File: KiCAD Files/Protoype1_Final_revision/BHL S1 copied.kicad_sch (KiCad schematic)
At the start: 94 parts, among them IC1 NUP2105LT1G, IC2 NUP2105LT1G, IC3 IR2136STRPBF, J2 Conn_01x03_Pin, J3 Conn_01x03_Pin, Q1 CSD19502Q5B, Q2 CSD19502Q5B, Q3 CSD19502Q5B, Q4 CSD19502Q5B, Q5 CSD19502Q5B, Q7 CSD19502Q5B, U1 ME6211C30M5, U2 SPX3819M5-L-5-0, U3 Solder Pad, U5 STM32G431CBU6, Y1 8MHz

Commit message: unlocked files
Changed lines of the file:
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@@
 	)
 	(global_label "Curr_fdbk1_OPAmp-"
-		(shape input)
+		(shape passive)
 		(at 45.72 184.15 180)
 		(fields_autoplaced yes)
@@
 		)
 		(property "Intersheetrefs" "${INTERSHEET_REFS}"
-			(at 23.4431 184.15 0)
+			(at 24.5544 184.15 0)
 			(effects
 				(font
@@
 	)
 	(global_label "Vshunt_2-"
-		(shape input)
+		(shape passive)
 		(at 313.69 96.52 180)
 		(fields_autoplaced yes)
@@
 		)
 		(property "Intersheetrefs" "${INTERSHEET_REFS}"
-			(at 300.6659 96.52 0)
+			(at 301.7772 96.52 0)
 			(effects
 				(font
@@
 	)
 	(global_label "Vshunt_3-"
-		(shape input)
+		(shape passive)
 		(at 95.25 194.31 0)
 		(fields_autoplaced yes)
@@
 		)
 		(property "Intersheetrefs" "${INTERSHEET_REFS}"
-			(at 108.2741 194.31 0)
+			(at 107.1628 194.31 0)
 			(effects
 				(font
@@
 	)
 	(global_label "Vshunt_3-"
-		(shape input)
+		(shape passive)
 		(at 340.36 86.36 90)
 		(fields_autoplaced yes)
@@
 		)
 		(property "Intersheetrefs" "${INTERSHEET_REFS}"
-			(at 340.36 73.3359 90)
+			(at 340.36 74.4472 90)
 			(effects
 				(font
@@
 	)
 	(global_label "Vshunt_1-"
-		(shape input)
+		(shape passive)
 		(at 255.27 83.82 180)
 		(fields_autoplaced yes)
@@
 		)
 		(property "Intersheetrefs" "${INTERSHEET_REFS}"
-			(at 242.2459 83.82 0)
+			(at 243.3572 83.82 0)
 			(effects
 				(font
@@
 	)
 	(global_label "Vshunt_2-"
-		(shape input)
+		(shape passive)
 		(at 95.25 189.23 0)
 		(fields_autoplaced yes)
@@
 		)
 		(property "Intersheetrefs" "${INTERSHEET_REFS}"
-			(at 108.2741 189.23 0)
+			(at 107.1628 189.23 0)
 			(effects
 				(font
@@
 	)
 	(global_label "Curr_fdbk1_OPAmp-"
-		(shape input)
+		(shape passive)
 		(at 74.93 66.04 180)
 		(fields_autoplaced yes)
@@
 		)
 		(property "Intersheetrefs" "${INTERSHEET_REFS}"
-			(at 52.6531 66.04 0)
+			(at 53.7644 66.04 0)
 			(effects
 				(font
@@
 	)
 	(global_label "Vshunt_1-"
-		(shape input)
+		(shape passive)
 		(at 95.25 184.15 0)
 		(fields_autoplaced yes)
@@
 		)
 		(property "Intersheetrefs" "${INTERSHEET_REFS}"
-			(at 108.2741 184.15 0)
+			(at 107.1628 184.15 0)
 			(effects
 				(font
@@
 	)
 	(global_label "Curr_fdbk3_OPAmp-"
-		(shape input)
+		(shape passive)
 		(at 45.72 194.31 180)
 		(fields_autoplaced yes)
@@
 		)
 		(property "Intersheetrefs" "${INTERSHEET_REFS}"
-			(at 23.4431 194.31 0)
+			(at 24.5544 194.31 0)
 			(effects
 				(font
@@
 	)
 	(global_label "Curr_fdbk2_OPAmp-"
-		(shape input)
+		(shape passive)
 		(at 45.72 189.23 180)
 		(fields_autoplaced yes)
@@
 		)
 		(property "Intersheetrefs" "${INTERSHEET_REFS}"
-			(at 23.4431 189.23 0)
-			(effects
-				(font
+			(at 24.5544 189.23 0)
+			(effects
+				(font

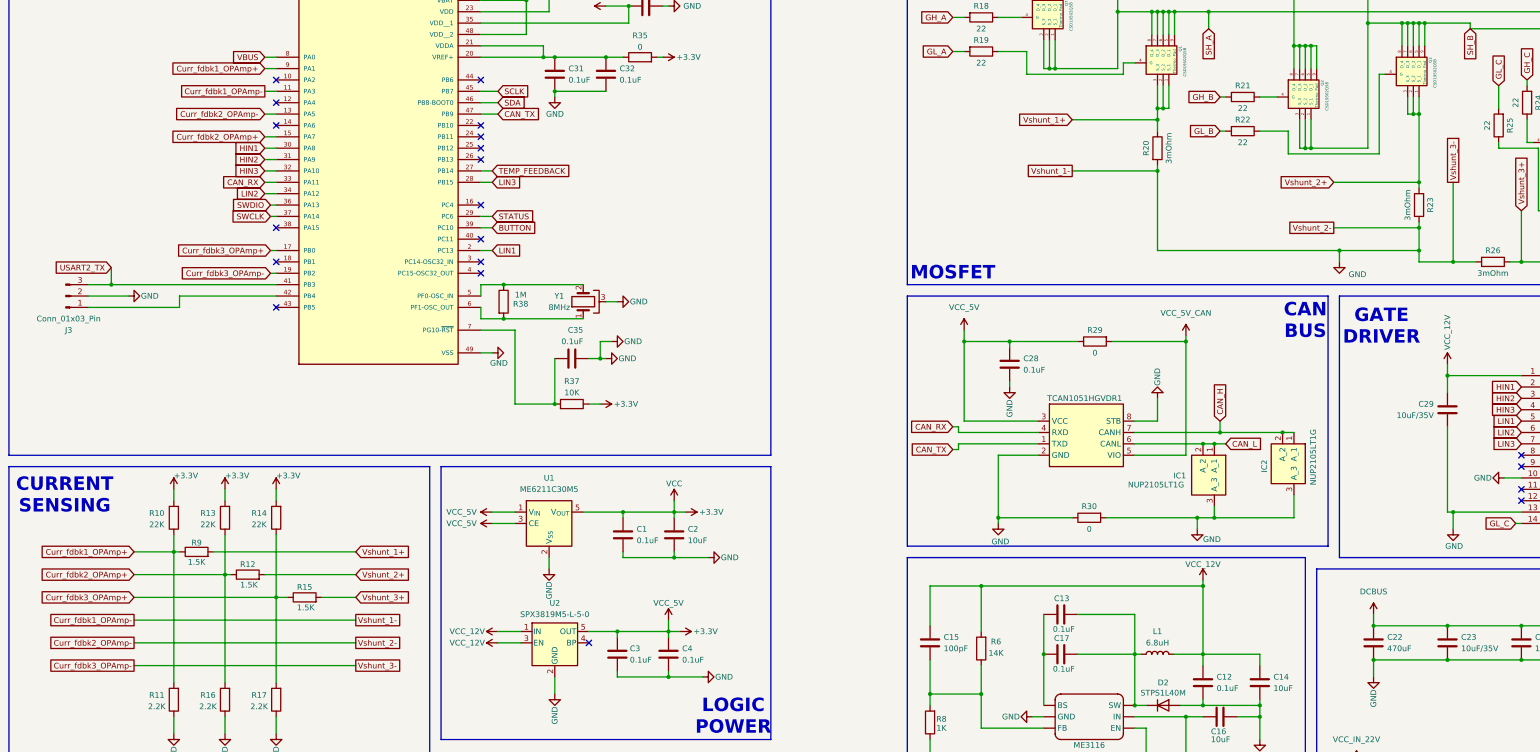
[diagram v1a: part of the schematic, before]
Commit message: Fixed GND Net label issue on PCB creation
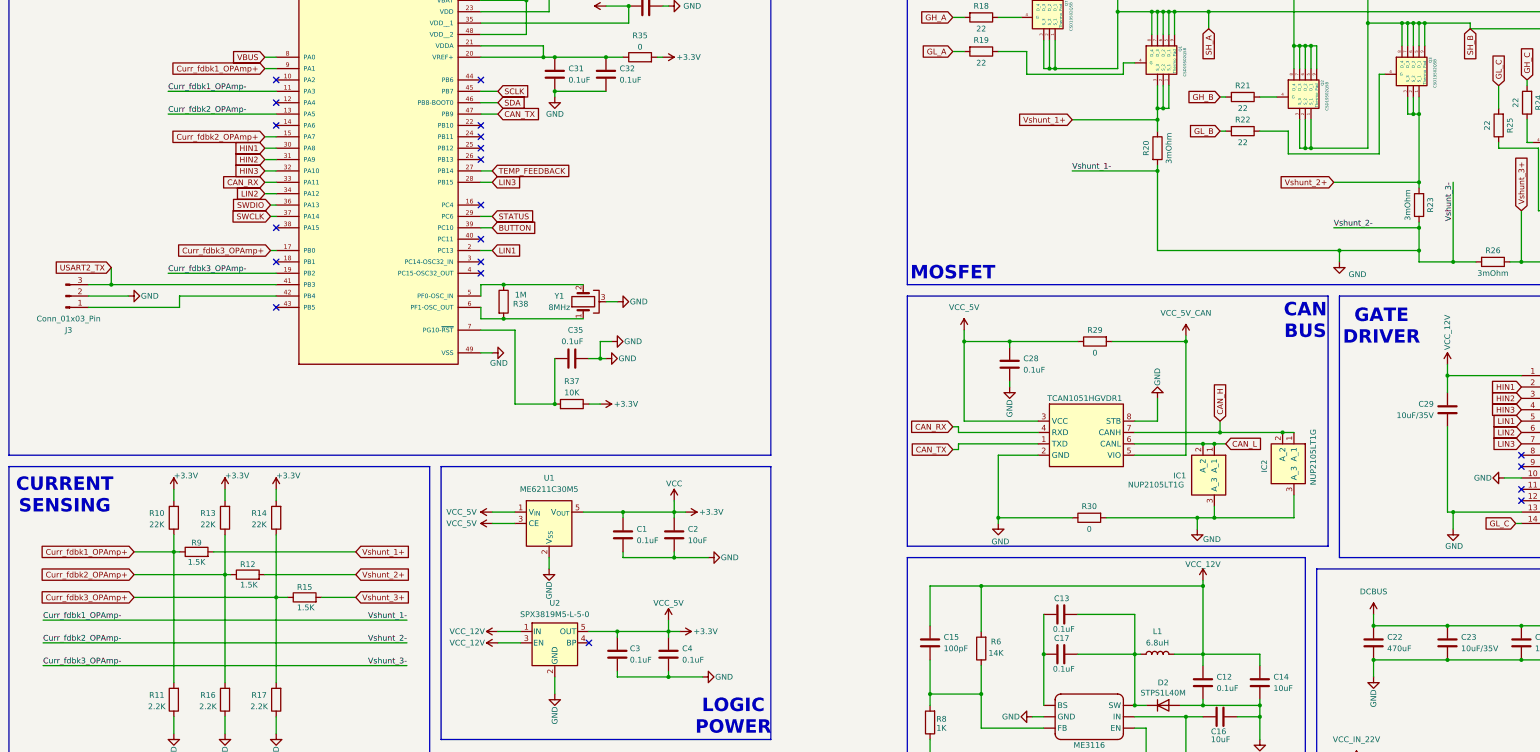
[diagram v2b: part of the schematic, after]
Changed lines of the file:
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@@
 	(wire
 		(pts
+			(xy 25.4 184.15) (xy 106.68 184.15)
+		)
+		(stroke
+			(width 0)
+			(type default)
+		)
+	)
+	(wire
+		(pts
 			(xy 153.67 195.58) (xy 153.67 196.85)
 		)
@@
 	(wire
 		(pts
-			(xy 45.72 189.23) (xy 95.25 189.23)
+			(xy 25.4 189.23) (xy 106.68 189.23)
 		)
 		(stroke
@@
 	(wire
 		(pts
-			(xy 45.72 194.31) (xy 95.25 194.31)
+			(xy 25.4 194.31) (xy 106.68 194.31)
 		)
 		(stroke
@@
 	(wire
 		(pts
-			(xy 45.72 184.15) (xy 95.25 184.15)
-		)
-		(stroke
-			(width 0)
-			(type default)
-		)
-	)
-	(wire
-		(pts
 			(xy 350.52 78.74) (xy 359.41 78.74)
 		)
@@
 	(wire
 		(pts
-			(xy 76.2 106.68) (xy 77.47 106.68)
+			(xy 53.34 106.68) (xy 77.47 106.68)
 		)
 		(stroke
@@
 	(wire
 		(pts
-			(xy 74.93 66.04) (xy 77.47 66.04)
+			(xy 53.34 66.04) (xy 77.47 66.04)
 		)
 		(stroke
@@
 	(wire
 		(pts
-			(xy 74.93 71.12) (xy 77.47 71.12)
+			(xy 53.34 71.12) (xy 77.47 71.12)
 		)
 		(stroke
@@
 		)
 	)
-	(global_label "Curr_fdbk1_OPAmp-"
-		(shape passive)
-		(at 45.72 184.15 180)
-		(fields_autoplaced yes)
+	(label "Vshunt_3-"
+		(at 340.36 86.36 270)
 		(effects
 			(font
 				(size 1.27 1.27)
 			)
-			(justify right)
+			(justify right bottom)
 		)
-		(property "Intersheetrefs" "${INTERSHEET_REFS}"
-			(at 24.5544 184.15 0)
-			(effects
-				(font
-					(size 1.27 1.27)
-				)
-				(justify right)
-				(hide yes)
+	)
+	(label "Curr_fdbk3_OPAmp-"
+		(at 53.34 106.68 0)
+		(effects
+			(font
+				(size 1.27 1.27)
+			)
+			(justify left bottom)
+		)
+	)
+	(label "Curr_fdbk3_OPAmp-"
+		(at 25.4 194.31 0)
+		(effects
+			(font
+				(size 1.27 1.27)
 			)
+			(justify left bottom)
+		)
+	)
+	(label "Curr_fdbk2_OPAmp-"
+		(at 25.4 189.23 0)
+		(effects
+			(font
+				(size 1.27 1.27)
+			)
+			(justify left bottom)
+		)
+	)
+	(label "Curr_fdbk1_OPAmp-"
+		(at 25.4 184.15 0)
+		(effects
+			(font
+				(size 1.27 1.27)
+			)
+			(justify left bottom)
+		)
+	)
+	(label "Curr_fdbk2_OPAmp-"
+		(at 53.34 71.12 0)
+		(effects
+			(font
+				(size 1.27 1.27)
+			)
+			(justify left bottom)
+		)
+	)
+	(label "Vshunt_1-"
+		(at 255.27 83.82 0)
+		(effects
+			(font
+				(size 1.27 1.27)
+			)
+			(justify left bottom)
+		)
+	)
+	(label "Vshunt_3-"
+		(at 106.68 194.31 180)
+		(effects
+			(font
+				(size 1.27 1.27)
+			)
+			(justify right bottom)
+		)
+	)
+	(label "Vshunt_1-"
+		(at 106.68 184.15 180)
+		(effects
+			(font
+				(size 1.27 1.27)
+			)
+			(justify right bottom)
+		)
+	)
+	(label "Vshunt_2-"
+		(at 313.69 96.52 0)
+		(effects
+			(font
+				(size 1.27 1.27)
+			)
+			(justify left bottom)
+		)
+	)
+	(label "Vshunt_2-"
+		(at 106.68 189.23 180)
+		(effects
+			(font
+				(size 1.27 1.27)
+			)
+			(justify right bottom)
+		)
+	)
+	(label "Curr_fdbk1_OPAmp-"
+		(at 53.34 66.04 0)
+		(effects
+			(font
+				(size 1.27 1.27)
+			)
+			(justify left bottom)
 		)
 	)
@@
 		)
 	)
-	(global_label "Vshunt_2-"
-		(shape passive)
-		(at 313.69 96.52 180)
-		(fields_autoplaced yes)
-		(effects
-			(font
-				(size 1.27 1.27)
-			)
-			(justify right)
-		)
-		(property "Intersheetrefs" "${INTERSHEET_REFS}"
-			(at 301.7772 96.52 0)
-			(effects
-				(font
-					(size 1.27 1.27)
-				)
-				(justify right)
-				(hide yes)
-			)
-		)
-	)
 	(global_label "SWCLK"
 		(shape input)
@@
 		)
 	)
-	(global_label "Vshunt_3-"
-		(shape passive)
-		(at 95.25 194.31 0)
-		(fields_autoplaced yes)
-		(effects
-			(font
-				(size 1.27 1.27)
-			)
-			(justify left)
-		)
-		(property "Intersheetrefs" "${INTERSHEET_REFS}"
-			(at 107.1628 194.31 0)
-			(effects
-				(font
-					(size 1.27 1.27)
-				)
-				(justify left)
-				(hide yes)
-			)
-		)
-	)
 	(global_label "VB3"
 		(shape input)
@@
 		)
 	)
-	(global_label "Vshunt_3-"
-		(shape passive)
-		(at 340.36 86.36 90)
-		(fields_autoplaced yes)
-		(effects
-			(font
-				(size 1.27 1.27)
-			)
-			(justify left)
-		)
-		(property "Intersheetrefs" "${INTERSHEET_REFS}"
-			(at 340.36 74.4472 90)
-			(effects
-				(font
-					(size 1.27 1.27)
-				)
-				(justify left)
-				(hide yes)
-			)
-		)
-	)
 	(global_label "Curr_fdbk2_OPAmp+"
 		(shape input)
@@
 		)
 	)
-	(global_label "Vshunt_1-"
-		(shape passive)
-		(at 255.27 83.82 180)
-		(fields_autoplaced yes)
-		(effects
-			(font
-				(size 1.27 1.27)
-			)
-			(justify right)
-		)
-		(property "Intersheetrefs" "${INTERSHEET_REFS}"
-			(at 243.3572 83.82 0)
-			(effects
-				(font
-					(size 1.27 1.27)
-				)
-				(justify right)
-				(hide yes)
-			)
-		)
-	)
 	(global_label "CAN_RX"
 		(shape input)
@@
 		)
 	)
-	(global_label "Vshunt_2-"
-		(shape passive)
-		(at 95.25 189.23 0)
-		(fields_autoplaced yes)
-		(effects
-			(font
-				(size 1.27 1.27)
-			)
-			(justify left)
-		)
-		(property "Intersheetrefs" "${INTERSHEET_REFS}"
-			(at 107.1628 189.23 0)
-			(effects
-				(font
-					(size 1.27 1.27)
-				)
-				(justify left)
-				(hide yes)
-			)
-		)
-	)
 	(global_label "SH_C"
 		(shape input)
@@
 		)
 	)
-	(global_label "Curr_fdbk1_OPAmp-"
-		(shape passive)
-		(at 74.93 66.04 180)
-		(fields_autoplaced yes)
-		(effects
-			(font
-				(size 1.27 1.27)
-			)
-			(justify right)
-		)
-		(property "Intersheetrefs" "${INTERSHEET_REFS}"
-			(at 53.7644 66.04 0)
-			(effects
-				(font
-					(size 1.27 1.27)
-				)
-				(justify right)
-				(hide yes)
-			)
-		)
-	)
 	(global_label "HIN2"
 		(shape input)
@@
 		)
 	)
-	(global_label "Vshunt_1-"
-		(shape passive)
-		(at 95.25 184.15 0)
-		(fields_autoplaced yes)
-		(effects
-			(font
-				(size 1.27 1.27)
-			)
-			(justify left)
-		)
-		(property "Intersheetrefs" "${INTERSHEET_REFS}"
-			(at 107.1628 184.15 0)
-			(effects
-				(font
-					(size 1.27 1.27)
-				)
-				(justify left)
-				(hide yes)
-			)
-		)
-	)
 	(global_label "SDA"
 		(shape input)
@@
 		)
 	)
-	(global_label "Curr_fdbk2_OPAmp-"
-		(shape input)
-		(at 74.93 71.12 180)
-		(fields_autoplaced yes)
-		(effects
-			(font
-				(size 1.27 1.27)
-			)
-			(justify right)
-		)
-		(property "Intersheetrefs" "${INTERSHEET_REFS}"
-			(at 52.6531 71.12 0)
-			(effects
-				(font
-					(size 1.27 1.27)
-				)
-				(justify right)
-				(hide yes)
-			)
-		)
-	)
 	(global_label "VBUS"
 		(shape input)
@@
 		)
 	)
-	(global_label "Curr_fdbk3_OPAmp-"
-		(shape passive)
-		(at 45.72 194.31 180)
-		(fields_autoplaced yes)
-		(effects
-			(font
-				(size 1.27 1.27)
-			)
-			(justify right)
-		)
-		(property "Intersheetrefs" "${INTERSHEET_REFS}"
-			(at 24.5544 194.31 0)
-			(effects
-				(font
-					(size 1.27 1.27)
-				)
-				(justify right)
-				(hide yes)
-			)
-		)
-	)
 	(global_label "SWDIO"
 		(shape input)
@@
 		)
 	)
-	(global_label "Curr_fdbk2_OPAmp-"
-		(shape passive)
-		(at 45.72 189.23 180)
-		(fields_autoplaced yes)
-		(effects
-			(font
-				(size 1.27 1.27)
-			)
-			(justify right)
-		)
-		(property "Intersheetrefs" "${INTERSHEET_REFS}"
-			(at 24.5544 189.23 0)
-			(effects
-				(font
-					(size 1.27 1.27)
-				)
-				(justify right)
-				(hide yes)
-			)
-		)
-	)
 	(global_label "GH_C"
 		(shape input)
@@
 				(hide yes)
 			)
-		)
-	)
-	(global_label "Curr_fdbk3_OPAmp-"
-		(shape input)
-		(at 76.2 106.68 180)
-		(fields_autoplaced yes)
-		(effects
-			(font
-				(size 1.27 1.27)
-			)
-			(justify right)
-		)
-		(property "Intersheetrefs" "${INTERSHEET_REFS}"
-			(at 53.9231 106.68 0)
-			(effects
-				(font
-					(size 1.27 1.27)
-				)
-				(justify right)
-				(hide yes)
-			)

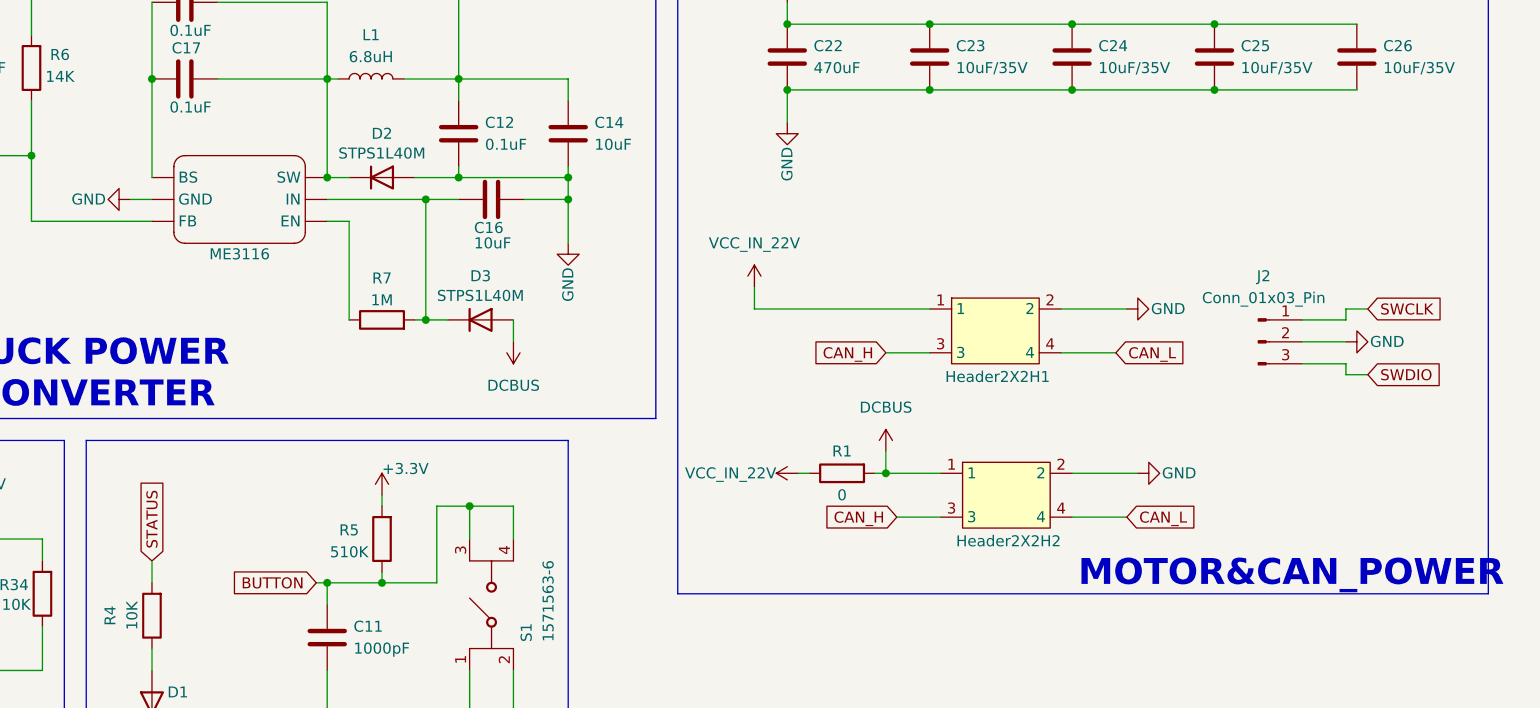
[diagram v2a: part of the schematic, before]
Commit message: Terminator block added, footprint error fixed, 9 schematic errors remains, may need to update all file paths of the symbol library.
Moo
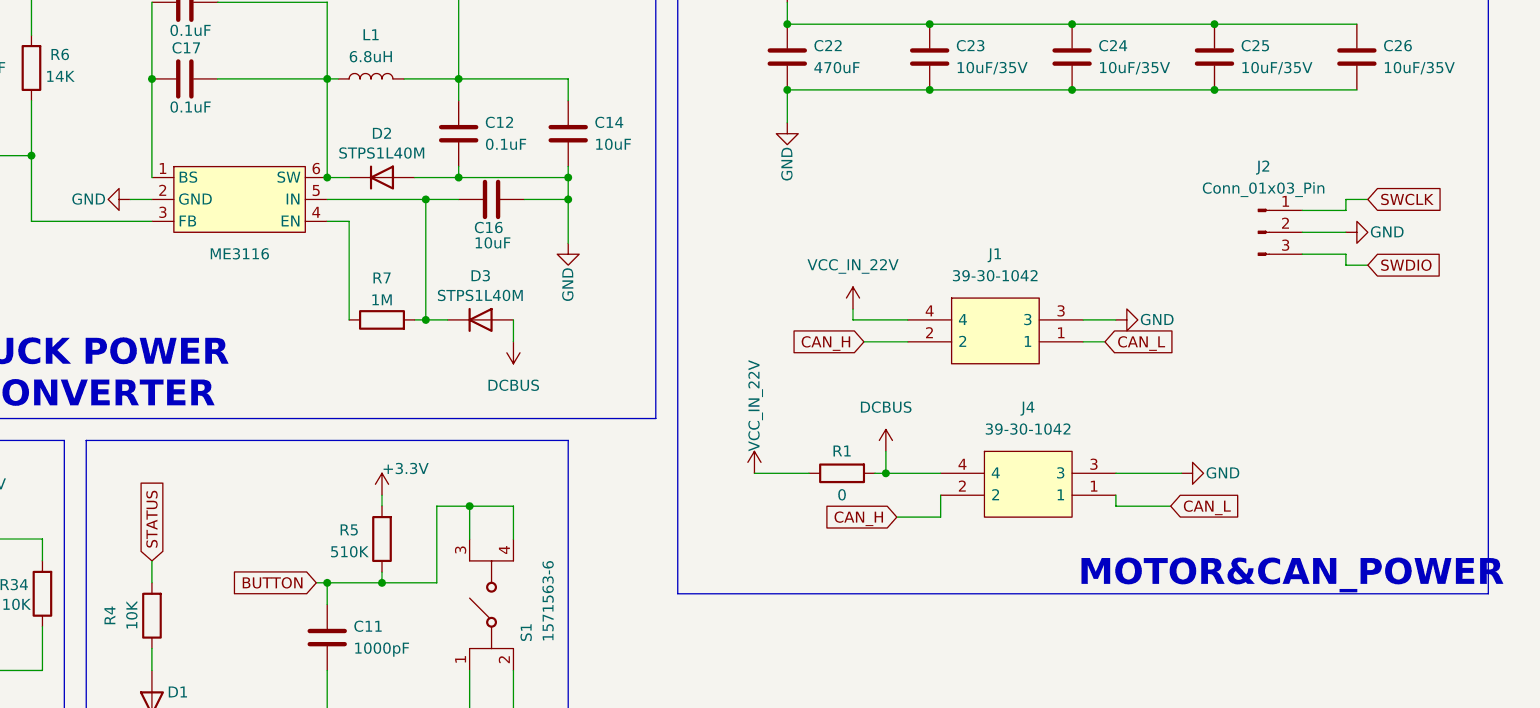
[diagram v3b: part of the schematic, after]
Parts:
- removed Header2X2H1, Header2X2H2: ~, Connector_PinHeader_2.54mm:PinHeader_2x02_P2.54mm_Vertical, symbol Buck converter:Header_2X2H
- added J1, J4: 39-30-1042, Footprint for BHL S1:Terminator, symbol Terminator:39-30-1042
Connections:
- net CAN_H: now also J1.2, J4.2
- net CAN_L: now also J1.1, J4.1
- net DCBUS: now also J4.4
- net GND: now also ME3116.2 (GND), J1.3, J4.3; no longer ME3116. (EN)
- net VCC_IN_22V: now also J1.4
- net at C15.2, R6.1, R8.2: now also ME3116.3 (FB); no longer ME3116. (EN)
- net at C13.1, C17.1: now also ME3116.1 (BS); no longer ME3116. (EN)
- net at C13.2, C17.2, D2.1 (K)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: now also ME3116.6 (SW); no longer ME3116. (EN)
- net at C16.2, D3.1 (K), R7.2: now also ME3116.5 (IN); no longer ME3116. (EN)
- net at R7.1: now also ME3116.4 (EN); no longer ME3116. (EN)
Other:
- moved on the sheet: J2

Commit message: Resonator footprint updated
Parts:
- Y1: footprint Footprint for BHL S1:CSTNE8M00G520000R0_Resonator -> Footprint for BHL S1:CSTNE8M00G55Z000R0_Resonator
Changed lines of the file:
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@@
 			)
 		)
-		(property "Footprint" "Footprint for BHL S1:CSTNE8M00G520000R0_Resonator"
+		(property "Footprint" "Footprint for BHL S1:CSTNE8M00G55Z000R0_Resonator"
 			(at 146.05 113.03 0)
 			(effects

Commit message: Worked on the PCB layout
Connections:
- net GND: now also J3.1 (Pin_1); no longer J3.2 (Pin_2)
- net at U5.42 (PB4): now also J3.2 (Pin_2); no longer J3.1 (Pin_1)
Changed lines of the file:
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@@
 	(wire
 		(pts
-			(xy 35.56 111.76) (xy 44.45 111.76)
+			(xy 35.56 111.76) (xy 77.47 111.76)
 		)
 		(stroke
@@
 	(wire
 		(pts
+			(xy 35.56 114.3) (xy 45.72 114.3)
+		)
+		(stroke
+			(width 0)
+			(type default)
+		)
+	)
+	(wire
+		(pts
 			(xy 269.24 182.88) (xy 269.24 191.77)
 		)
@@
 	(wire
 		(pts
-			(xy 55.88 114.3) (xy 35.56 114.3)
-		)
-		(stroke
-			(width 0)
-			(type default)
-		)
-	)
-	(wire
-		(pts
 			(xy 146.05 271.78) (xy 146.05 274.32)
 		)
@@
 	(wire
 		(pts
-			(xy 55.88 111.76) (xy 55.88 114.3)
-		)
-		(stroke
-			(width 0)
-			(type default)
-		)
-	)
-	(wire
-		(pts
 			(xy 265.43 60.96) (xy 251.46 60.96)
 		)
@@
 	(wire
 		(pts
-			(xy 77.47 111.76) (xy 55.88 111.76)
-		)
-		(stroke
-			(width 0)
-			(type default)
-		)
-	)
-	(wire
-		(pts
 			(xy 367.03 241.3) (xy 360.68 241.3)
 		)
@@
 	(symbol
 		(lib_id "power:GND")
-		(at 44.45 111.76 90)
+		(at 45.72 114.3 90)
 		(mirror x)
 		(unit 1)
@@
 		(dnp no)
 		(property "Reference" "#PWR019"
-			(at 50.8 111.76 0)
+			(at 52.07 114.3 0)
 			(effects
 				(font
@@
 		)
 		(property "Value" "GND"
-			(at 47.244 111.76 90)
+			(at 48.514 114.3 90)
 			(effects
 				(font
@@
 		)
 		(property "Footprint" ""
-			(at 44.45 111.76 0)
+			(at 45.72 114.3 0)
 			(effects
 				(font
@@
 		)
 		(property "Datasheet" ""
-			(at 44.45 111.76 0)
+			(at 45.72 114.3 0)
 			(effects
 				(font
@@
 		)
 		(property "Description" "Power symbol creates a global label with name \"GND\" , ground"
-			(at 44.45 111.76 0)
+			(at 45.72 114.3 0)
 			(effects
 				(font
